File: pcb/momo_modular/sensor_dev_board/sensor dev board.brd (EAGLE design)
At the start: 100 x 80 mm, 9 parts

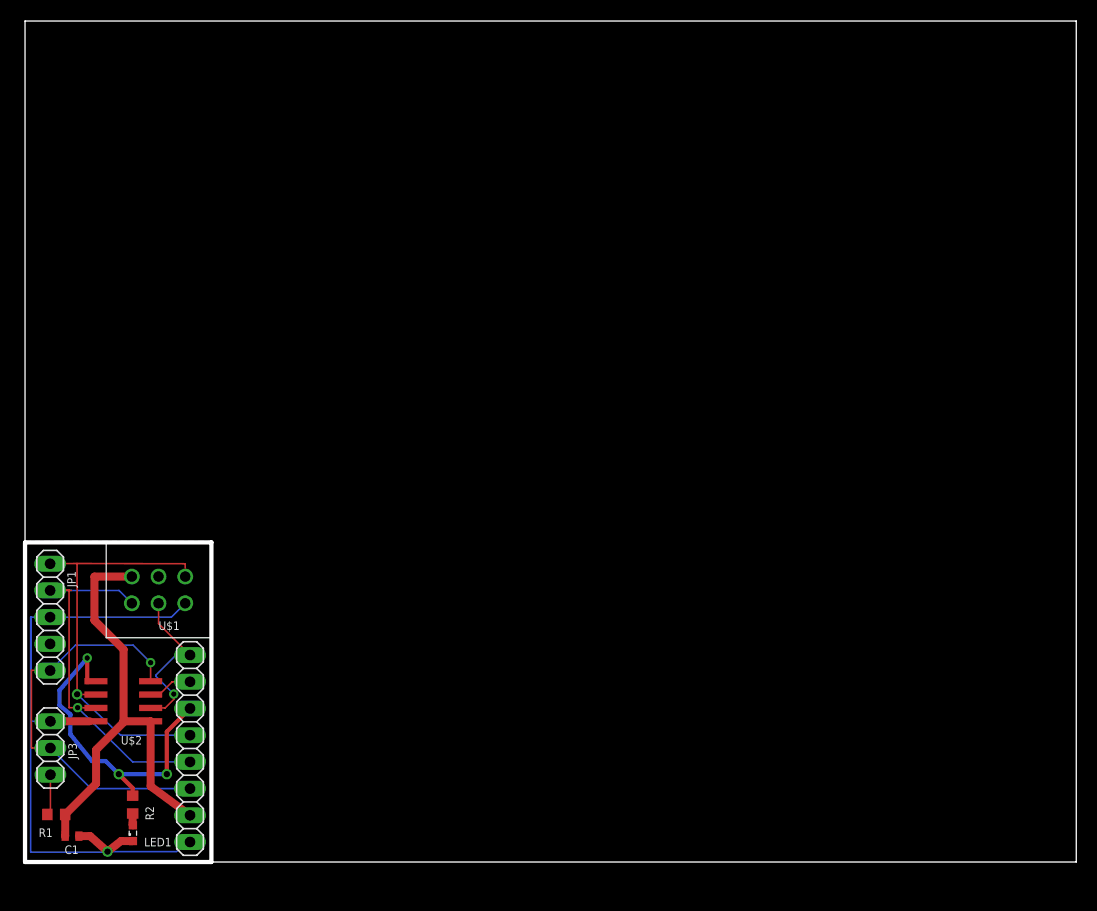
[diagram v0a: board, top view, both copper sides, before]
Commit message: Changed I2C Data line and added second indicator LED on 2.8V line
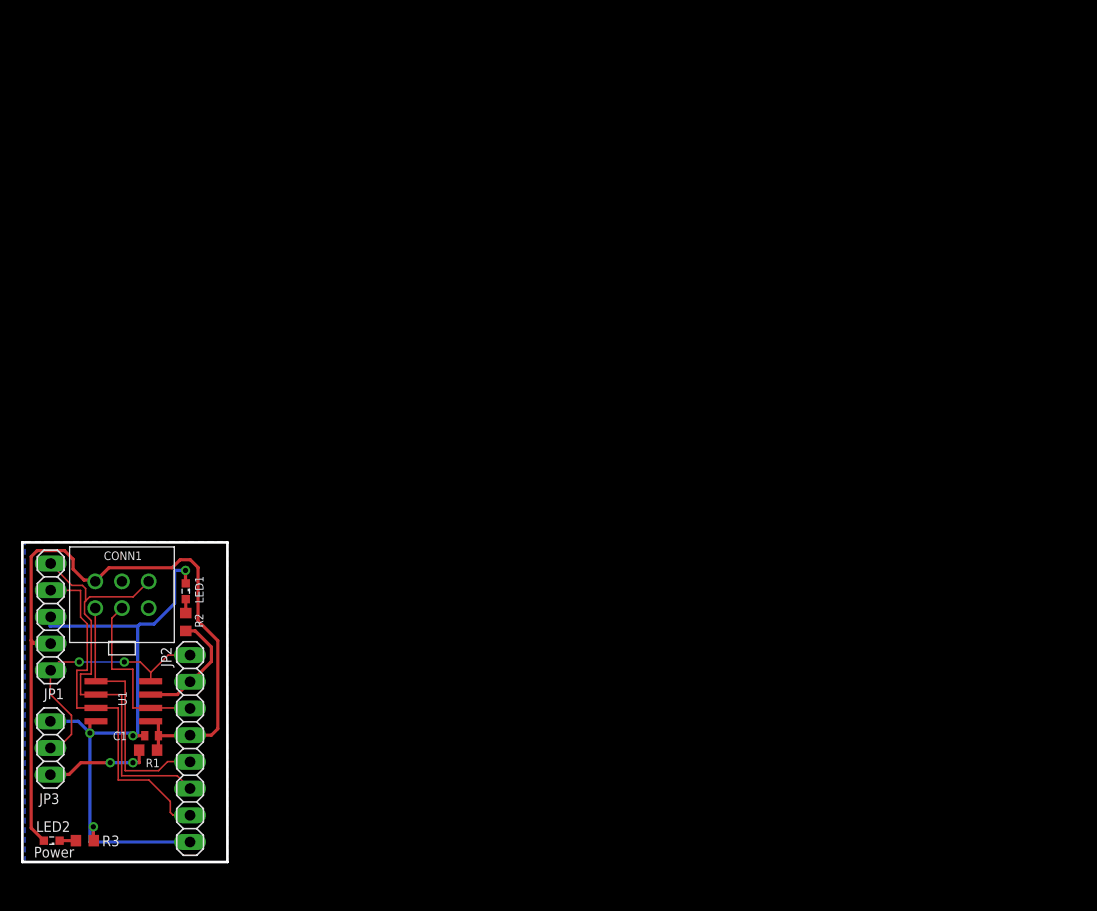
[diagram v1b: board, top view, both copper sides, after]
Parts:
- removed U$1: 2X3-MOLEX-90130, components:2X3-MOLEX-90130
- added CONN1: MOMO-SENSOR-HEADER, components:2X3-MOLEX-90130
- added LED2: (no value), led:SML0603
- added R3: 60, resistor:R0603
- moved LED1 23.6 mm to (15.3, 25.8), turned to 270 degrees
- moved R2 18.1 mm to (15.3, 22.8), turned to 270 degrees
- moved C1 12.2 mm to (12.0, 12.0), turned to 180 degrees
- moved R1 10.7 mm to (11.7, 10.6)
- moved JP1 0.06 mm to (2.44, 23.3)
- renumbered U$2 to U1
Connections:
- removed net N$3: JP2.6, R2.2, U1.5
- removed net N$5: JP1.4, JP2.4, U$1.4, U1.7
- removed net N$6: JP1.1, JP2.3, JP3.2, U1.4
- removed net N$7: JP2.8, U$1.5, U1.2
- removed net N$8: JP1.5, JP2.5, U$1.3, U1.6
- new net MCLR: JP1.1, JP2.8, JP3.2, U1.4
- new net RA0: JP1.4, JP2.2, U1.7
- new net RA1: CONN1.3, JP1.5, JP2.3, U1.6
- new net RA2: CONN1.4, JP2.4, U1.5
- new net RA4: JP2.7, R2.2, U1.3
- new net RA5: CONN1.5, JP2.6, U1.2
- net GND: now also R3.1; no longer U$1.6
- net N$2: now also LED2.C, R3.2; no longer JP2.7, U1.3
- net V+: now also CONN1.2; no longer U$1.2
- net VCCINT: now also CONN1.1, JP1.2, JP2.5, LED2.A; no longer JP2.2, U$1.1
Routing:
- net RA1: track 0.00 -> 41.1 mm
- net N$8: track 40.6 -> 0.00 mm, vias 1 -> 0
- net N$6: track 38.9 -> 0.00 mm, vias 1 -> 0
- net N$5: track 38.7 -> 0.00 mm, vias 1 -> 0
- net RA0: track 0.00 -> 34.9 mm
- net N$3: track 32.5 -> 0.00 mm, vias 3 -> 0
- net VCCINT: track 45.1 -> 74.2 mm
- net MCLR: track 0.00 -> 25.0 mm, vias 0 -> 2
- net RA2: track 0.00 -> 24.9 mm
- net RA5: track 0.00 -> 17.4 mm
- net N$7: track 15.7 -> 0.00 mm, vias 1 -> 0
- net GND: track 75.2 -> 62.5 mm, vias 1 -> 4
- net RA4: track 0.00 -> 11.5 mm
- net N$10: track 3.91 -> 10.2 mm, vias 0 -> 2
- net N$2: track 4.26 -> 1.55 mm
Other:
- board size 100 x 80 mm -> 19.5 x 30.4 mm
- board text added: "Power"

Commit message: minor changes
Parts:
- C1: value (none) -> 100 nF
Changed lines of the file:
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@@
 <attribute name="NAME" x="11.4808" y="9.017" size="0.8128" layer="25"/>
 </element>
-<element name="C1" library="rcl" package="C0402" value="" x="12.0396" y="12.0142" smashed="yes" rot="R180">
+<element name="C1" library="rcl" package="C0402" value="100 nF" x="12.0396" y="12.0142" smashed="yes" rot="R180">
 <attribute name="NAME" x="9.7028" y="12.3952" size="0.8128" layer="25" rot="R180"/>
-<attribute name="VALUE" x="12.6746" y="13.9192" size="1.27" layer="27" rot="R180"/>
 </element>
 <element name="R2" library="resistor" package="R0603" value="60" x="15.2908" y="22.8346" smashed="yes" rot="R270">

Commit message: Finalized the following boards for fabrication/assembly: Sensor Dev Board GSM Module Combined Wallpower and Controller Boards
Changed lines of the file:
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@@
 <grid distance="0.01" unitdist="inch" unit="inch" style="lines" multiple="1" display="no" altdistance="0.025" altunitdist="inch" altunit="inch"/>
 <layers>
-<layer number="1" name="Top" color="4" fill="1" visible="yes" active="yes"/>
-<layer number="16" name="Bottom" color="1" fill="1" visible="yes" active="yes"/>
-<layer number="17" name="Pads" color="2" fill="1" visible="yes" active="yes"/>
-<layer number="18" name="Vias" color="2" fill="1" visible="yes" active="yes"/>
+<layer number="1" name="Top" color="4" fill="1" visible="no" active="yes"/>
+<layer number="16" name="Bottom" color="1" fill="1" visible="no" active="yes"/>
+<layer number="17" name="Pads" color="2" fill="1" visible="no" active="yes"/>
+<layer number="18" name="Vias" color="2" fill="1" visible="no" active="yes"/>
 <layer number="19" name="Unrouted" color="6" fill="1" visible="yes" active="yes"/>
 <layer number="20" name="Dimension" color="15" fill="1" visible="yes" active="yes"/>
@@
 </element>
 <element name="C1" library="rcl" package="C0402" value="100 nF" x="12.0396" y="12.0142" smashed="yes" rot="R180">
-<attribute name="NAME" x="9.7028" y="12.3952" size="0.8128" layer="25" rot="R180"/>
+<attribute name="NAME" x="11.4808" y="12.3952" size="0.8128" layer="25" rot="R180"/>
 </element>
 <element name="R2" library="resistor" package="R0603" value="60" x="15.2908" y="22.8346" smashed="yes" rot="R270">

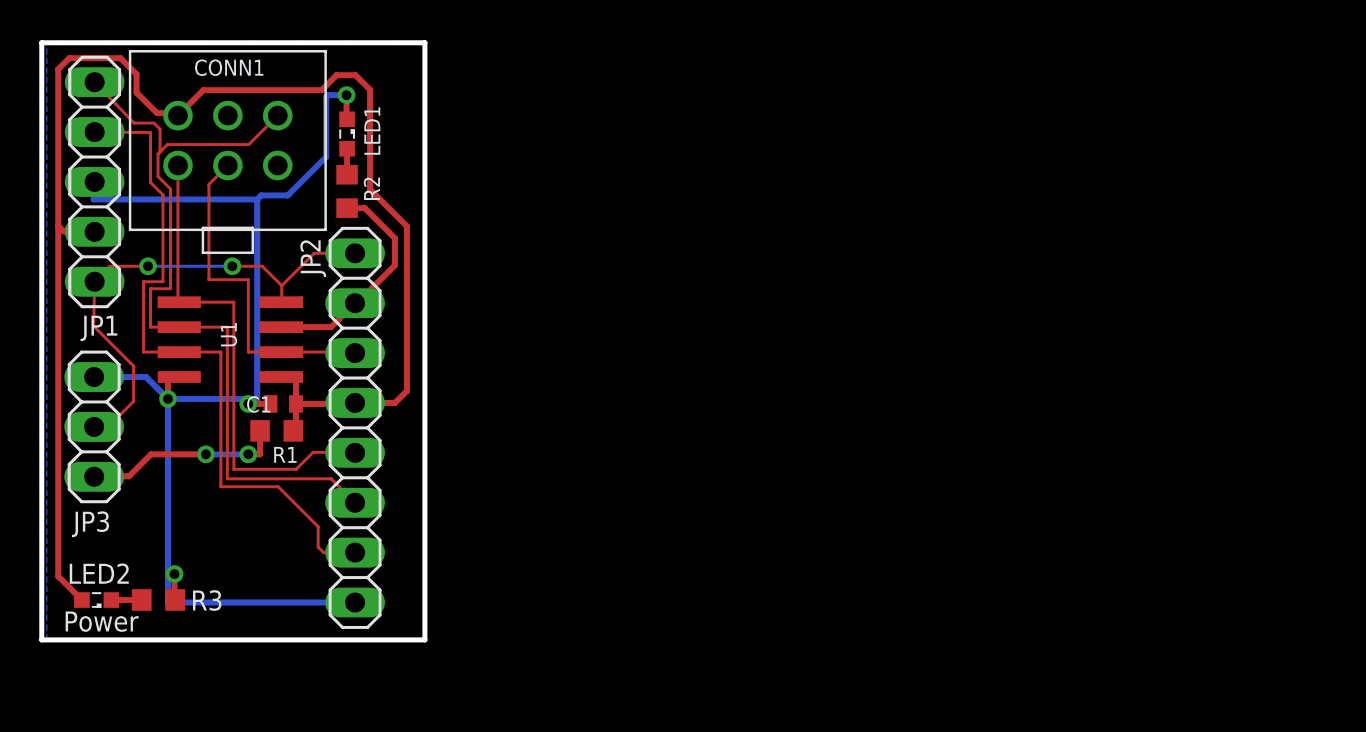
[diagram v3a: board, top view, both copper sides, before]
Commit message: Finished next version of hardware.  Working on automatic BOM generation for purchasing.
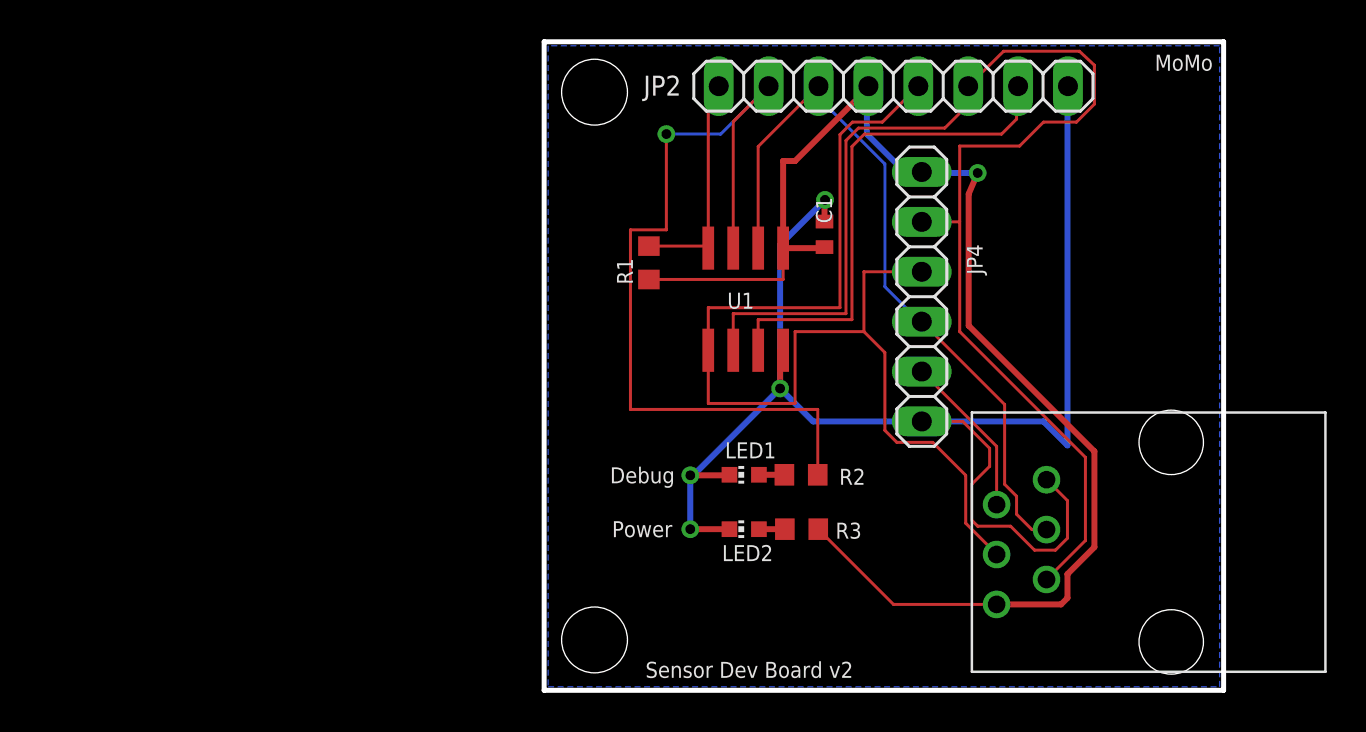
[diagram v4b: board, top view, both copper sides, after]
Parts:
- removed CONN1: MOMO-SENSOR-HEADER, components:2X3-MOLEX-90130
- removed JP1: (no value), pinhead:1X05
- removed JP3: (no value), pinhead:1X03
- added JP4: MOMO-VERT-6M, components:1X06
- added JP5: MOMO-SENSOR-RJ11, components:RJ-12
- LED1, LED2: device led:SML0603 -> led:CHIP-LED0603
- R2, R3: value 60 -> 62R
- moved LED2 33.2 mm to (35.5, 5.64), turned to 90 degrees
- moved R3 32.9 mm to (38.4, 5.64), turned to 0 degrees
- moved JP2 32.5 mm to (43.1, 28.2), turned to 180 degrees
- moved C1 28.9 mm to (39.6, 20.7), turned to 90 degrees
- moved R2 27.2 mm to (38.4, 8.41), turned to 0 degrees
- moved LED1 26.6 mm to (35.5, 8.41), turned to 90 degrees
- moved U1 26.3 mm to (35.6, 17.3), turned to 180 degrees
- moved R1 20.8 mm to (30.7, 19.2), turned to 270 degrees
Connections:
- removed net N$10: JP3.3, R1.1
- net GND: now also JP4.7, JP5.6, LED2.C; no longer JP1.3, JP3.1, R3.1
- net MCLR: now also R1.1; no longer JP1.1, JP3.2
- net N$2: now also LED2.A, R3.1; no longer LED2.C, R3.2
- net RA0: no longer JP1.4
- net RA1: now also JP4.3, JP5.2; no longer CONN1.3, JP1.5
- net RA2: now also JP4.4, JP5.3; no longer CONN1.4
- net RA5: now also JP4.5, JP5.4; no longer CONN1.5
- net V+: now also JP4.6, JP5.5; no longer CONN1.2
- net VCCINT: now also JP4.1, JP5.1, R3.2; no longer CONN1.1, JP1.2, LED2.A
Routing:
- net RA2: track 24.9 -> 58.2 mm
- net RA4: track 11.5 -> 43.9 mm, vias 0 -> 1
- net RA1: track 41.1 -> 69.0 mm
- net RA5: track 17.4 -> 37.4 mm
- net GND: track 62.5 -> 78.4 mm
- net MCLR: track 25.0 -> 11.5 mm, vias 2 -> 0
- net N$10: track 10.2 -> 0.00 mm, vias 2 -> 0
- net RA0: track 34.9 -> 25.8 mm
- net V+: track 0.00 -> 8.35 mm
- net VCCINT: track 74.2 -> 70.1 mm, vias 0 -> 1
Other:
- board size 19.5 x 30.4 mm -> 34.6 x 33 mm
- board text added: "Debug"
- board text added: "MoMo"
- board text added: "Sensor Dev Board v2"
